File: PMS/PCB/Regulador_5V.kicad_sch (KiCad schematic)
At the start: 14 parts, among them U1 MP2303ADN

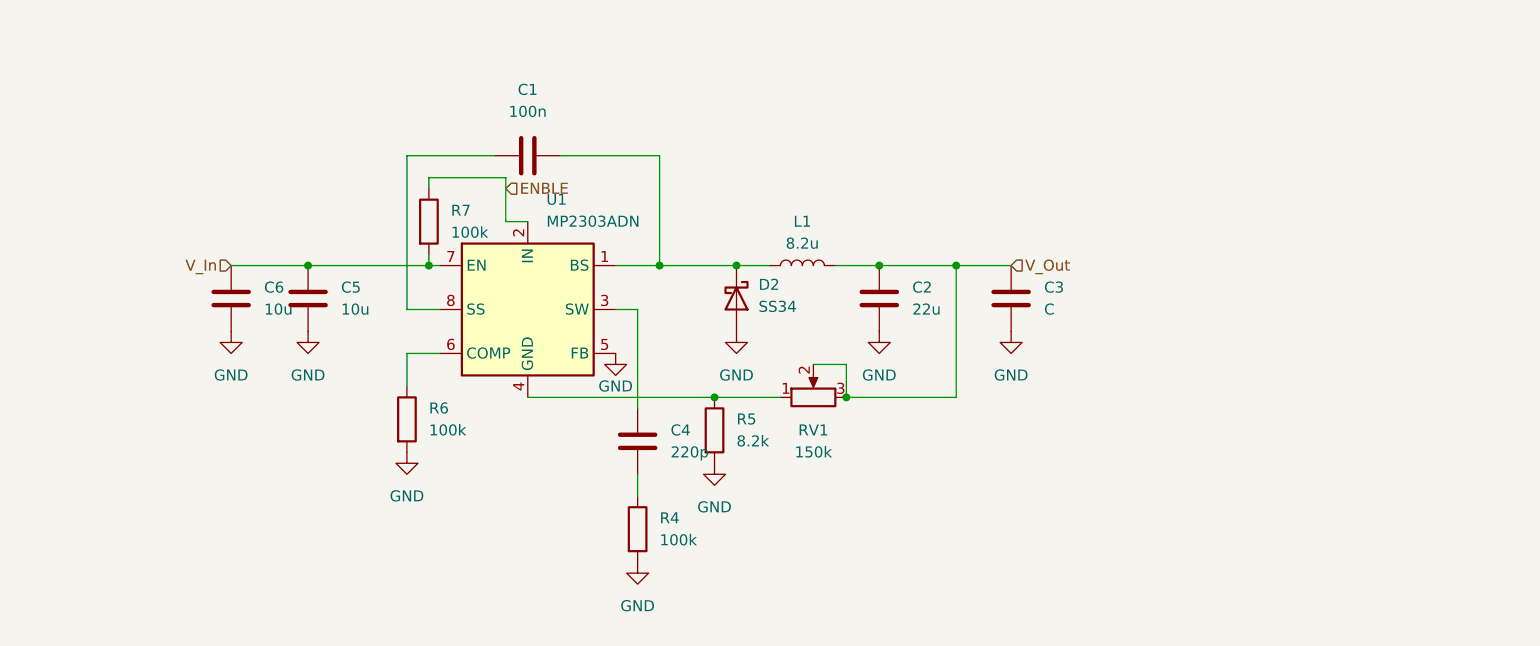
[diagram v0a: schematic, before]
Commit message: Define ciertos pines y diseña mediciones
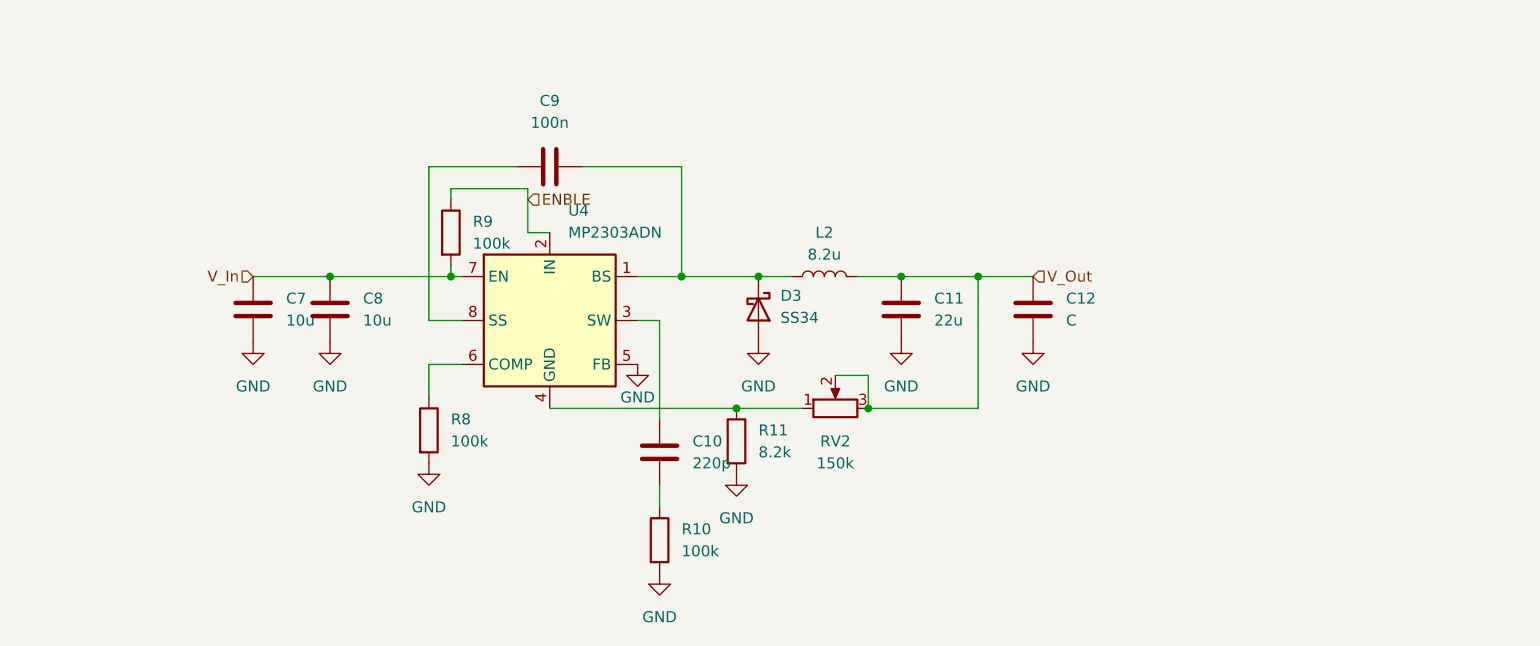
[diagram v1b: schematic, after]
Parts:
- removed C1: 100n, symbol Device:C
- removed C2: 22u, symbol Device:C
- removed C3: C, symbol Device:C
- removed C4: 220p, symbol Device:C
- removed C5, C6: 10u, symbol Device:C
- removed D2: SS34, Diode_SMD:D_SMA, symbol Diode:SS34
- removed L1: 8.2u, symbol Device:L
- removed R4, R6, R7: 100k, symbol Device:R
- removed R5: 8.2k, symbol Device:R
- removed RV1: 150k, symbol Device:R_Potentiometer
- removed U1: MP2303ADN, Package_SO:SOIC-8-1EP_3.9x4.9mm_P1.27mm_EP2.62x3.51mm, symbol Regulator_Switching:MP2303ADN
- added C10: 220p, symbol Device:C
- added C11: 22u, symbol Device:C
- added C12: C, symbol Device:C
- added C7, C8: 10u, symbol Device:C
- added C9: 100n, symbol Device:C
- added D3: SS34, Diode_SMD:D_SMA, symbol Diode:SS34
- added L2: 8.2u, symbol Device:L
- added R10, R8, R9: 100k, symbol Device:R
- added R11: 8.2k, symbol Device:R
- added RV2: 150k, symbol Device:R_Potentiometer
- added U4: MP2303ADN, Package_SO:SOIC-8-1EP_3.9x4.9mm_P1.27mm_EP2.62x3.51mm, symbol Regulator_Switching:MP2303ADN
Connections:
- net ENBLE: now also R9.1, U4.2 (IN)
- net GND: now also C11.2, C12.2, C7.2, C8.2, D3.2 (A), R10.2, R11.2, R8.2, U4.5 (FB)
- net V_In: now also C7.1, C8.1, R9.2, U4.7 (EN)
- net V_Out: now also C11.1, C12.1, L2.2, RV2.2, RV2.3
- new net: C9.2, D3.1 (K), L2.1, U4.1 (BS)
- new net: C9.1, U4.8 (SS)
- new net: R11.1, RV2.1, U4.4 (GND)
- new net: C10.2, R10.1
- new net: C10.1, U4.3 (SW)
- new net: R8.1, U4.6 (COMP)

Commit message: Continua Desarrollo
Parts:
- removed D3: SS34, Diode_SMD:D_SMA, symbol Diode:SS34
- removed RV2: 150k, symbol Device:R_Potentiometer
- removed U4: MP2303ADN, Package_SO:SOIC-8-1EP_3.9x4.9mm_P1.27mm_EP2.62x3.51mm, symbol Regulator_Switching:MP2303ADN
- added D3: SS34, symbol Device:D_Schottky
- added F2: Polyfuse, symbol Device:Polyfuse
- added R17, R7: 100K, symbol Device:R
- added U1: MP1584, Package_SO:SOIC-8-1EP_3.9x4.9mm_P1.27mm_EP2.62x3.51mm, symbol CubeSat:MP1584EN
- C10: value 220p -> 0.1n
- C11: value 22u -> 10u
- C12: value C -> 100n
- C7: value 10u -> 100n
- L2: value 8.2u -> 4.7u
- R10: value 100k -> 8K2
- R11: value 8.2k -> 43K
- R8: value 100k -> R
- R9: value 100k -> 100K
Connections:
- net GND: now also R9.2, D3.2 (A), R17.2, U1.5 (GND); no longer R11.2
- net V_In: now also R7.2, U1.7 (VIN); no longer R9.2
- net V_Out: now also F2.2; no longer C11.1, C12.1, L2.2
- net at C9.2, L2.1: now also D3.1 (K), U1.1 (SW)
- net at C9.1: now also U1.8 (BS)
- net at R11.1: now also R10.1, U1.4 (FB)
- net at C10.2: now also R17.1; no longer R10.1
- net at C10.1: now also U1.3 (COMP)
- net EN: now reaches R8.1
- net EN: now also R7.1, U1.2 (EN)
- net ENBLE: no longer names the net of R9.1
- net ENBLE: now also U1.6 (FREQ)
- new net: C11.1, C12.1, F2.1, L2.2, R11.2

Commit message: Correcciones menores
mentirillas
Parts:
- removed R8: R, symbol Device:R
- added Q301: IRF9630, symbol Simulation_SPICE:PMOS
- renumbered C9 to C301, C7 to C302, C8 to C303, C11 to C304, C12 to C305, C10 to C306, D3 to D301, F2 to F301, L2 to L301, R7 to R301, R11 to R302, R9 to R303, R10 to R304, R17 to R305, U1 to U301
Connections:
- net EN: now also Q301.2 (G); no longer R301.1, U301.2 (EN)
- net V_Out: now also Q301.1 (D); no longer F301.2
- net V_In renamed VSYS
- new net: R301.1, U301.2 (EN)
- new net V_Out_SB: F301.2, Q301.3 (S)
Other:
- company: (none) -> Misión LAMBDA
- title: (none) -> PMS - Regulador 5V
